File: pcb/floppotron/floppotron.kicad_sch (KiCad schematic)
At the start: 60 parts, among them J1 DIN-5_180degree, J11 Conn_01x02, J2 Conn_01x02, J3 Conn_01x02, J4 Conn_01x02, J5 Conn_01x02, J6 Conn_01x02, J7 Conn_01x02, J9 USB_B, Q1 BC817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

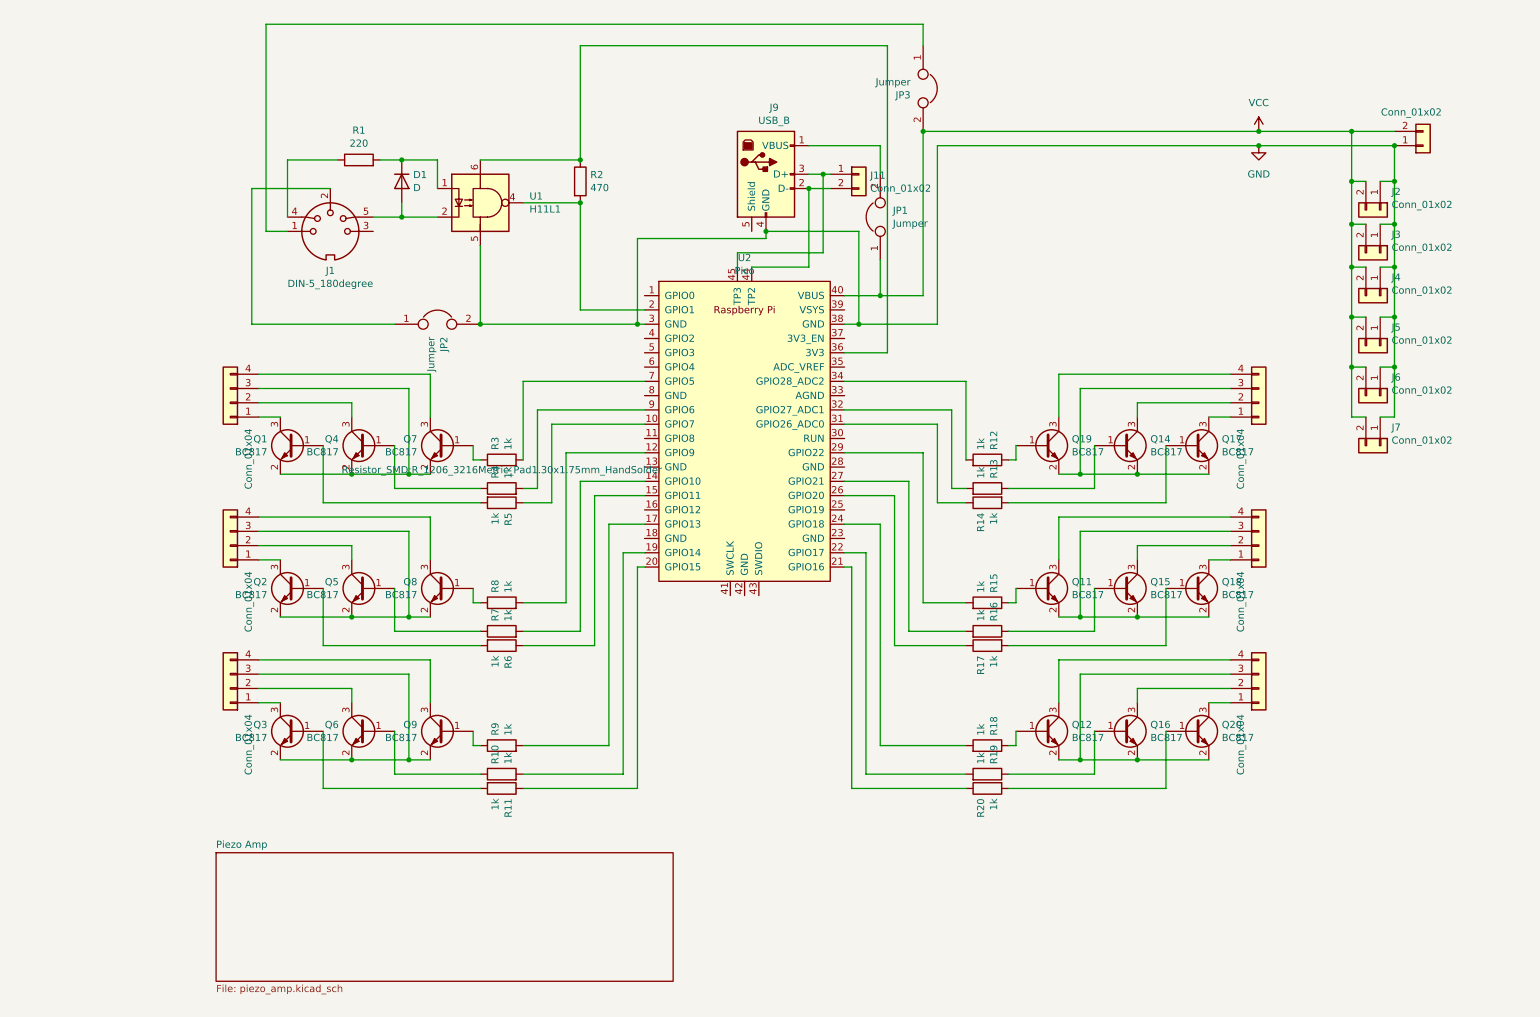
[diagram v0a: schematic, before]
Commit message: redesign pcb for pico W
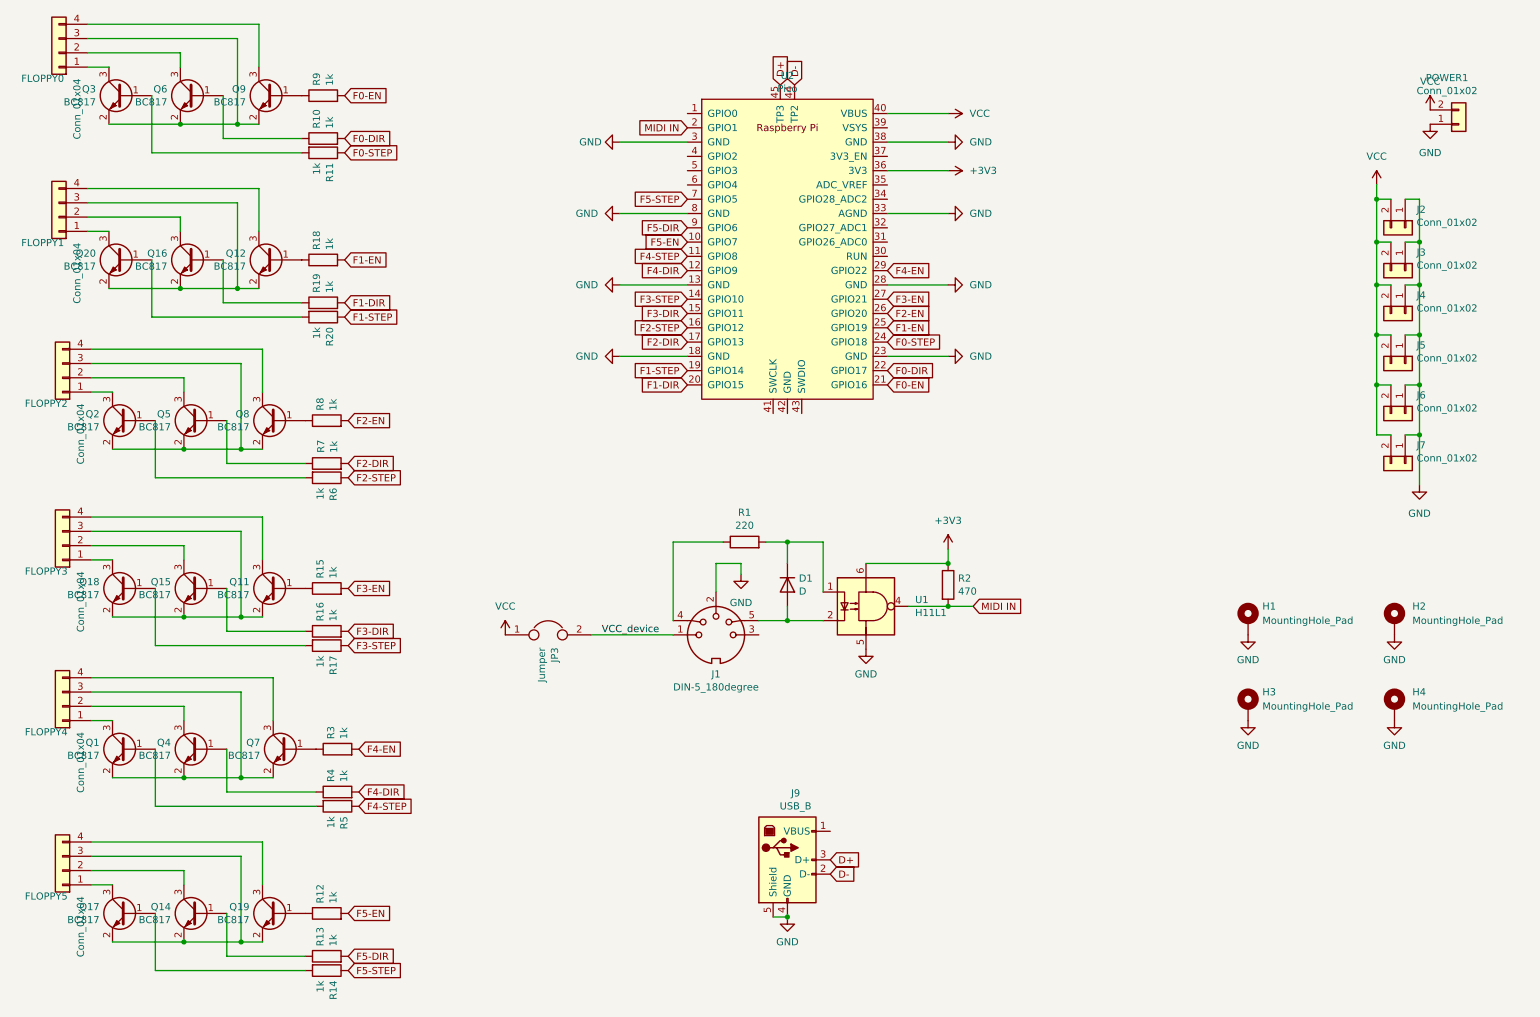
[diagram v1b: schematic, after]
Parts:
- removed J11: Conn_01x02, Connector_JST:JST_XH_B2B-XH-A_1x02_P2.50mm_Vertical, symbol Connector_Generic:Conn_01x02
- removed JP1, JP2: Jumper, Connector_PinHeader_2.54mm:PinHeader_1x02_P2.54mm_Vertical, symbol floppotron-rescue:Jumper-Device
- added H1, H2, H3, H4: MountingHole_Pad, MountingHole:MountingHole_3.2mm_M3_DIN965_Pad, symbol Mechanical:MountingHole_Pad
- R1, R2: footprint Resistor_THT:R_Axial_DIN0204_L3.6mm_D1.6mm_P5.08mm_Horizontal -> Resistor_SMD:R_1206_3216Metric_Pad1.30x1.75mm_HandSolder
- U2: footprint pico:RPi_Pico_SMD_TH -> kicad-parts:RPi_Pico_debug_hole_USB_SMD_TH
- gave numbers to parts that had none: 7
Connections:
- net GND: now also J1.2, J9.5 (Shield), U2.13 (GND), U2.18 (GND), U2.23 (GND), U2.28 (GND), U2.33 (AGND), U2.8 (GND), H1.1, H2.1, H3.1, H4.1
- net VCC: now also JP3.1; no longer JP3.2
- net F4-STEP: now reaches R5.1
- net F4-STEP: now also U2.11 (GPIO8); no longer U2.10 (GPIO7)
- net F2-EN: now reaches R8.2
- net F2-EN: now also U2.26 (GPIO20); no longer U2.12 (GPIO9)
- net F2-DIR: now reaches R7.2
- net F2-DIR: now also U2.17 (GPIO13); no longer U2.14 (GPIO10)
- net F2-STEP: now reaches R6.1
- net F2-STEP: now also U2.16 (GPIO12); no longer U2.15 (GPIO11)
- net F0-EN: now reaches R9.2
- net F0-EN: now also U2.21 (GPIO16); no longer U2.17 (GPIO13)
- net F0-DIR: now reaches R10.2
- net F0-DIR: now also U2.22 (GPIO17); no longer U2.19 (GPIO14)
- net MIDI IN: now reaches R2.2, U1.4, U2.2 (GPIO1)
- net F0-STEP: now reaches R11.1
- net F0-STEP: now also U2.24 (GPIO18); no longer U2.20 (GPIO15)
- net F1-STEP: now reaches R20.1
- net F1-STEP: now also U2.19 (GPIO14); no longer U2.21 (GPIO16)
- net F1-DIR: now reaches R19.2
- net F1-DIR: now also U2.20 (GPIO15); no longer U2.22 (GPIO17)
- net F1-EN: now reaches R18.2
- net F1-EN: now also U2.25 (GPIO19); no longer U2.24 (GPIO18)
- net F3-STEP: now reaches R17.1
- net F3-STEP: now also U2.14 (GPIO10); no longer U2.26 (GPIO20)
- net F3-DIR: now reaches R16.2
- net F3-DIR: now also U2.15 (GPIO11); no longer U2.27 (GPIO21)
- net F3-EN: now reaches R15.2
- net F3-EN: now also U2.27 (GPIO21); no longer U2.29 (GPIO22)
- net at U2.31 (GPIO26_ADC0): no longer R14.1
- net at U2.32 (GPIO27_ADC1): no longer R13.2
- net at U2.34 (GPIO28_ADC2): no longer R12.2
- net +3V3: now reaches R2.1, U1.6, U2.36 (3V3)
- net D-: now reaches J9.2 (D-), U2.44 (TP2)
- net D+: now reaches J9.3 (D+), U2.45 (TP3)
- net F4-EN: now reaches R3.2
- net F4-EN: now also U2.29 (GPIO22); no longer U2.7 (GPIO5)
- net F4-DIR: now reaches R4.2
- net F4-DIR: now also U2.12 (GPIO9); no longer U2.9 (GPIO6)
- net VCC_device: now reaches J1.1
- net VCC_device: now also JP3.2; no longer JP3.1
- new net F5-DIR: R13.2, U2.9 (GPIO6)
- new net F5-EN: R12.2, U2.10 (GPIO7)
- new net F5-STEP: R14.1, U2.7 (GPIO5)
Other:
- removed sheet Piezo Amp
- moved on the sheet: D1, J1, J2, J3, J4, J5, J6, J7, J9, JP3, Q1, Q11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

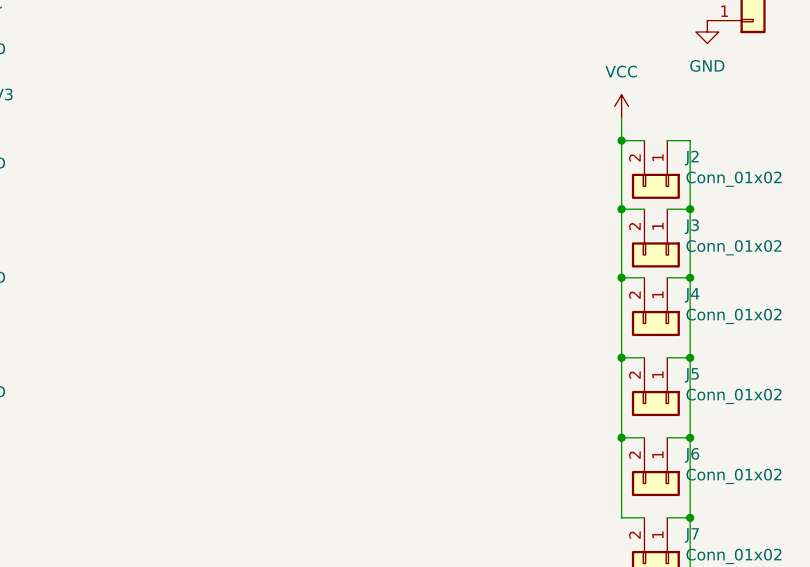
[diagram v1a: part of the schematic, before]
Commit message: pcb: add kosmo power connector
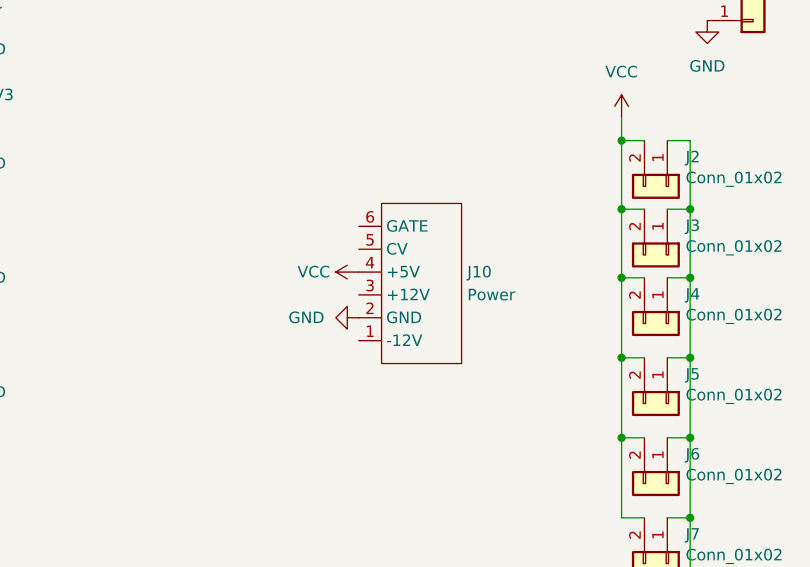
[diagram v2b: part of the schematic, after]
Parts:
- added J10: Power, kosmo:Power 16 Pin, symbol kosmo:Power-16
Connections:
- net GND: now also J10.2 (GND)
- net VCC: now also J10.4 (+5V)
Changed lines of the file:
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@@
+    )
+  )
+  (symbol (lib_id "kosmo:Power-16") (at 234.315 66.04 0) (unit 1)
+    (in_bom yes) (on_board yes) (dnp no) (fields_autoplaced)
+    (property "Reference" "J10" (at 240.03 64.77 0)
+      (effects (font (size 1.27 1.27)) (justify left))
+    )
+    (property "Value" "Power" (at 240.03 67.31 0)
+      (effects (font (size 1.27 1.27)) (justify left))
+    )
+    (property "Footprint" "kosmo:Power 16 Pin" (at 240.665 63.5 90)
+      (effects (font (size 1.27 1.27)) hide)
+    )
+    (property "Datasheet" "" (at 236.855 59.69 0)
+      (effects (font (size 1.27 1.27)) hide)
+    )
+    (pin "6")
+    (pin "5")
+    (pin "1")
+    (pin "3")
+    (pin "2")
+    (pin "4")
+    (instances
+      (project "floppotron"
+        (path "/97adfaa4-8f8a-4db9-ae33-a9b1ecf3b12d"
+          (reference "J10") (unit 1)
+        )
+      )
     )
   )
@@
     )
   )
+  (symbol (lib_id "power:GND") (at 227.965 69.85 270) (unit 1)
+    (in_bom yes) (on_board yes) (dnp no) (fields_autoplaced)
+    (property "Reference" "#PWR022" (at 221.615 69.85 0)
+      (effects (font (size 1.27 1.27)) hide)
+    )
+    (property "Value" "GND" (at 224.155 69.85 90)
+      (effects (font (size 1.27 1.27)) (justify right))
+    )
+    (property "Footprint" "" (at 227.965 69.85 0)
+      (effects (font (size 1.27 1.27)) hide)
+    )
+    (property "Datasheet" "" (at 227.965 69.85 0)
+      (effects (font (size 1.27 1.27)) hide)
+    )
+    (pin "1")
+    (instances
+      (project "floppotron"
+        (path "/97adfaa4-8f8a-4db9-ae33-a9b1ecf3b12d"
+          (reference "#PWR022") (unit 1)
+        )
+      )
+    )
+  )
   (symbol (lib_id "power:VCC") (at 180.975 34.925 270) (unit 1)
     (in_bom yes) (on_board yes) (dnp no) (fields_autoplaced)
@@
         )
       )
+    )
+  )
+  (symbol (lib_id "power:VCC") (at 227.965 64.77 90) (unit 1)
+    (in_bom yes) (on_board yes) (dnp no) (fields_autoplaced)
+    (property "Reference" "#PWR023" (at 231.775 64.77 0)
+      (effects (font (size 1.27 1.27)) hide)
+    )
+    (property "Value" "VCC" (at 224.79 64.77 90)
+      (effects (font (size 1.27 1.27)) (justify left))
+    )
+    (property "Footprint" "" (at 227.965 64.77 0)
+      (effects (font (size 1.27 1.27)) hide)
+    )
+    (property "Datasheet" "" (at 227.965 64.77 0)
+      (effects (font (size 1.27 1.27)) hide)
+    )
+    (pin "1")
+    (instances
+      (project "floppotron"
+        (path "/97adfaa4-8f8a-4db9-ae33-a9b1ecf3b12d"
+          (reference "#PWR023") (unit 1)
+        )
+      )
